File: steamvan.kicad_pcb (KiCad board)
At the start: 2 copper layers, 243.4 x 76.7 mm, 168 parts, among them J1 Conn_01x05_Male, Q1 FMMT493TA, SW1 SW_Push, U1 STM32F303CBTx, U2 TLV70233_SOT23-5, U3 NUF2221W1T2G, Y1 8MHz

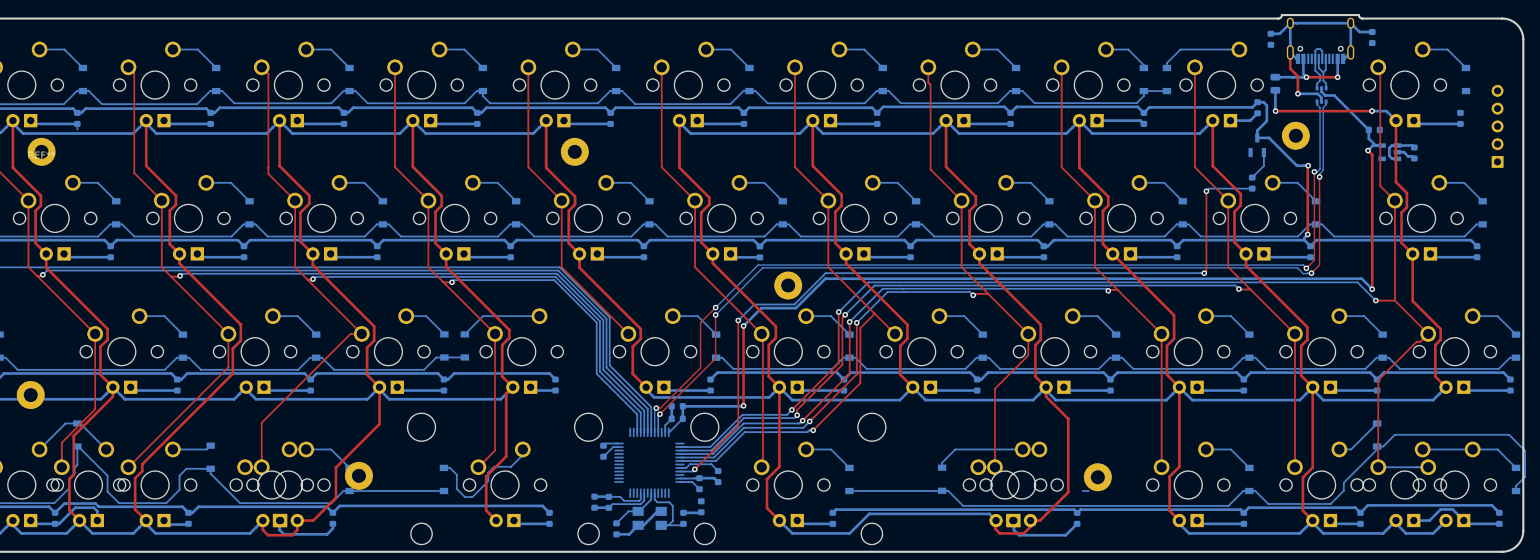
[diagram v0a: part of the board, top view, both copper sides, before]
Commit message: Update: Add schematic components for RGB underglow, and work on routing
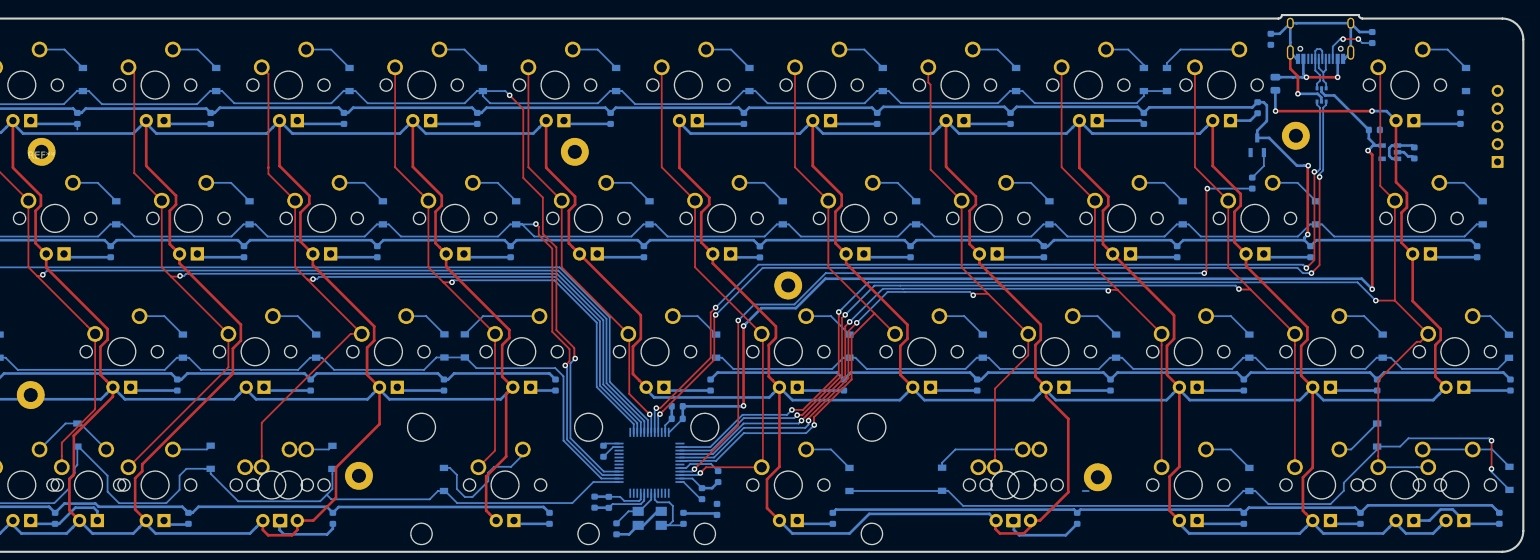
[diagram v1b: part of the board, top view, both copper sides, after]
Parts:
- moved D40 3.99 mm to (144.4, 118.3)
- moved C9 2.29 mm to (199.4, 125.7)
- moved C3 1.47 mm to (197.2, 123.5)
- moved D36 1.01 mm to (312.5, 102.4)
- moved D46 0.95 mm to (312.6, 121.3)
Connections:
- U1 pad 13: COL1 -> ROW3
- U1 pad 14: Net-(U1-Pad14) -> ROW2
- U1 pad 15: Net-(U1-Pad15) -> ROW1
- U1 pad 16: COL5 -> ROW0
- U1 pad 17: COL7 -> RGBLED_3V3
- U1 pad 18: ROW0 -> Net-(U1-Pad18)
- U1 pad 19: ROW1 -> Net-(U1-Pad19)
- U1 pad 20: ROW2 -> Net-(U1-Pad20)
- U1 pad 26: Net-(U1-Pad26) -> COL4
- U1 pad 27: COL4 -> COL3
- U1 pad 28: COL3 -> COL2
- U1 pad 29: COL2 -> COL1
- U1 pad 30: COL1 -> COL0
- U1 pad 31: COL0 -> COL5
- U1 pad 46: Net-(U1-Pad46) -> COL6
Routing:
- net ROW0: track 188.1 -> 254.2 mm, vias 0 -> 2
- net ROW1: track 232.5 -> 278.0 mm, vias 0 -> 2
- net ROW2: track 193.1 -> 226.7 mm
- net ROW3: track 198.4 -> 225.7 mm, vias 0 -> 2
- net COL5: track 44.0 -> 59.4 mm, vias 0 -> 1
- net COL6: track 63.2 -> 75.4 mm, vias 0 -> 1
- net Net-(RC7-Pad2): track 0.00 -> 8.06 mm, vias 0 -> 2
- net Net-(D40-Pad2): track 9.66 -> 6.34 mm
- net GND: track 71.8 -> 74.8 mm
- net Net-(D36-Pad2): track 7.28 -> 6.28 mm
- net Net-(D46-Pad2): track 14.4 -> 13.4 mm
- net +3V3: track 173.1 -> 174.1 mm
- net COL11: track 187.8 -> 188.7 mm

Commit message: Update: Work on underglow
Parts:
- added C12: 100n, Capacitor_SMD:C_0603_1608Metric, B.Cu at (153.0, 111.5)
- added C13: 100n, Capacitor_SMD:C_0603_1608Metric, B.Cu at (100.2, 113.4)
- added C14: 100n, Capacitor_SMD:C_0603_1608Metric, B.Cu at (98.3, 78.2)
- added C15: 100n, Capacitor_SMD:C_0603_1608Metric, B.Cu at (138.3, 78.0)
- added C16: 100n, Capacitor_SMD:C_0603_1608Metric, B.Cu at (195.6, 77.9)
- added C17: 100n, Capacitor_SMD:C_0603_1608Metric, B.Cu at (234.6, 77.5)
- added C18: 100n, Capacitor_SMD:C_0603_1608Metric, B.Cu at (271.8, 78.2)
- added C19: 100n, Capacitor_SMD:C_0603_1608Metric, B.Cu at (284.6, 113.8)
- added C20: 100n, Capacitor_SMD:C_0603_1608Metric, B.Cu at (231.4, 116.0)
- added RC9: 470, Resistor_SMD:R_0603_1608Metric, B.Cu at (166.8, 114.2)
- added RGB1: WS2812B, LED_SMD:LED_WS2812B_PLCC4_5.0x5.0mm_P3.2mm, B.Cu at (150.0, 115.6)
- added RGB2: WS2812B, LED_SMD:LED_WS2812B_PLCC4_5.0x5.0mm_P3.2mm, B.Cu at (94.7, 114.8)
- added RGB3: WS2812B, LED_SMD:LED_WS2812B_PLCC4_5.0x5.0mm_P3.2mm, B.Cu at (92.8, 79.0)
- added RGB4: WS2812B, LED_SMD:LED_WS2812B_PLCC4_5.0x5.0mm_P3.2mm, B.Cu at (132.7, 78.9)
- added RGB5: WS2812B, LED_SMD:LED_WS2812B_PLCC4_5.0x5.0mm_P3.2mm, B.Cu at (190.0, 79.0)
- added RGB6: WS2812B, LED_SMD:LED_WS2812B_PLCC4_5.0x5.0mm_P3.2mm, B.Cu at (228.5, 79.0)
- added RGB7: WS2812B, LED_SMD:LED_WS2812B_PLCC4_5.0x5.0mm_P3.2mm, B.Cu at (266.3, 79.0)
- added RGB8: WS2812B, LED_SMD:LED_WS2812B_PLCC4_5.0x5.0mm_P3.2mm, B.Cu at (278.1, 114.3)
- added RGB9: WS2812B, LED_SMD:LED_WS2812B_PLCC4_5.0x5.0mm_P3.2mm, B.Cu at (225.9, 119.5)
- added U4: 74LVC1G34, Package_TO_SOT_SMD:SOT-353_SC-70-5, B.Cu at (175.8, 118.6)
- moved Q1 13.4 mm to (289.6, 77.0), turned to 270 degrees
- moved D20 1.13 mm to (227.6, 84.5)
- moved D15 1.11 mm to (132.6, 84.5)
- moved D22 1.11 mm to (265.9, 84.5)
- moved D18 0.98 mm to (189.7, 84.3)
- moved D13 0.98 mm to (92.1, 84.3)
- moved Y1 0.38 mm to (189.7, 127.4)
- moved C1 0.36 mm to (185.0, 128.1)
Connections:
- U1 pad 4: ROW3 -> Net-(U1-Pad4)
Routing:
- net Net-(RGB1-Pad2): track 0.00 -> 64.2 mm
- net GND: track 74.8 -> 135.1 mm
- net Net-(RGB4-Pad2): track 0.00 -> 53.6 mm
- net Net-(RGB2-Pad2): track 0.00 -> 44.6 mm, vias 0 -> 2
- net Net-(RGB3-Pad2): track 0.00 -> 36.4 mm
- net Net-(RGB5-Pad2): track 0.00 -> 34.9 mm
- net Net-(RGB6-Pad2): track 0.00 -> 34.3 mm
- net RGBLED: track 0.00 -> 20.7 mm
- net Net-(Q1-Pad1): track 4.26 -> 15.8 mm
- net Net-(RC9-Pad2): track 0.00 -> 10.7 mm
- net +5V: track 1298.2 -> 1307.4 mm
- net RGBLED_3V3: track 0.00 -> 9.07 mm, vias 0 -> 2
- net Net-(RC6-Pad2): track 0.00 -> 8.20 mm, vias 0 -> 2
- net ROW1: track 278.0 -> 270.3 mm
- net LEDGND: track 833.7 -> 836.7 mm, vias 2 -> 3
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
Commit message: Update: Work on routing
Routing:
- net Net-(RGB7-Pad2): track 0.00 -> 59.6 mm, vias 0 -> 2
- net Net-(RGB8-Pad2): track 0.00 -> 59.4 mm
- net ROW2: track 226.7 -> 250.6 mm, vias 0 -> 2
- net GND: track 135.1 -> 157.3 mm
- net +5V: track 1307.4 -> 1324.9 mm
- net LEDPWM: track 111.9 -> 112.5 mm

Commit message: Update: More work on routing
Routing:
- net SWCLK: track 0.00 -> 160.4 mm, vias 0 -> 2
- net Net-(RC8-Pad1): track 12.4 -> 154.0 mm, vias 0 -> 2
- net +5V: track 1324.9 -> 1309.8 mm
- net COL1: track 168.1 -> 177.7 mm

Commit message: Update: More routing
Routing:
- net NRST: track 0.00 -> 179.1 mm, vias 0 -> 1
- net +3V3: track 174.2 -> 346.2 mm, vias 4 -> 10
- net SWDIO: track 0.00 -> 159.3 mm, vias 0 -> 3
- net LEDGND: track 836.7 -> 976.5 mm, vias 3 -> 12
- net GND: track 157.3 -> 277.0 mm, vias 1 -> 5
- net ROW0: track 254.2 -> 299.0 mm, vias 2 -> 4
- net ROW3: track 225.9 -> 261.5 mm, vias 2 -> 4
- net +5V: track 1309.8 -> 1326.4 mm, vias 2 -> 4
- net Net-(D41-Pad2): track 18.2 -> 12.4 mm
- net Net-(RGB3-Pad2): track 36.4 -> 37.9 mm
- net Net-(RGB7-Pad2): track 59.6 -> 58.8 mm
- net Net-(K_Q1-Pad4): track 7.66 -> 6.86 mm
- net COL11: track 189.0 -> 188.3 mm
- net COL10: track 159.7 -> 160.3 mm

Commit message: Update: Finish routing
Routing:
- net GND: track 277.0 -> 629.9 mm, vias 5 -> 28
- net +5V: track 1326.4 -> 1330.8 mm, vias 4 -> 5
- net NRST: track 179.1 -> 180.0 mm
- net D_N: track 133.9 -> 133.3 mm

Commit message: Update: Work on ground plane
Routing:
- net +5V: track 1330.8 -> 1340.2 mm
- net COL10: track 160.3 -> 164.2 mm
- net COL9: track 140.1 -> 141.8 mm
- net COL7: track 85.0 -> 86.6 mm
- net COL11: track 188.5 -> 189.9 mm
- net COL2: track 152.2 -> 153.4 mm
- net COL1: track 177.7 -> 178.7 mm
- net COL8: track 126.3 -> 127.2 mm
- net GND: vias 28 -> 87
- added copper zone on B.Cu, net GND
- added copper zone on F.Cu, net GND

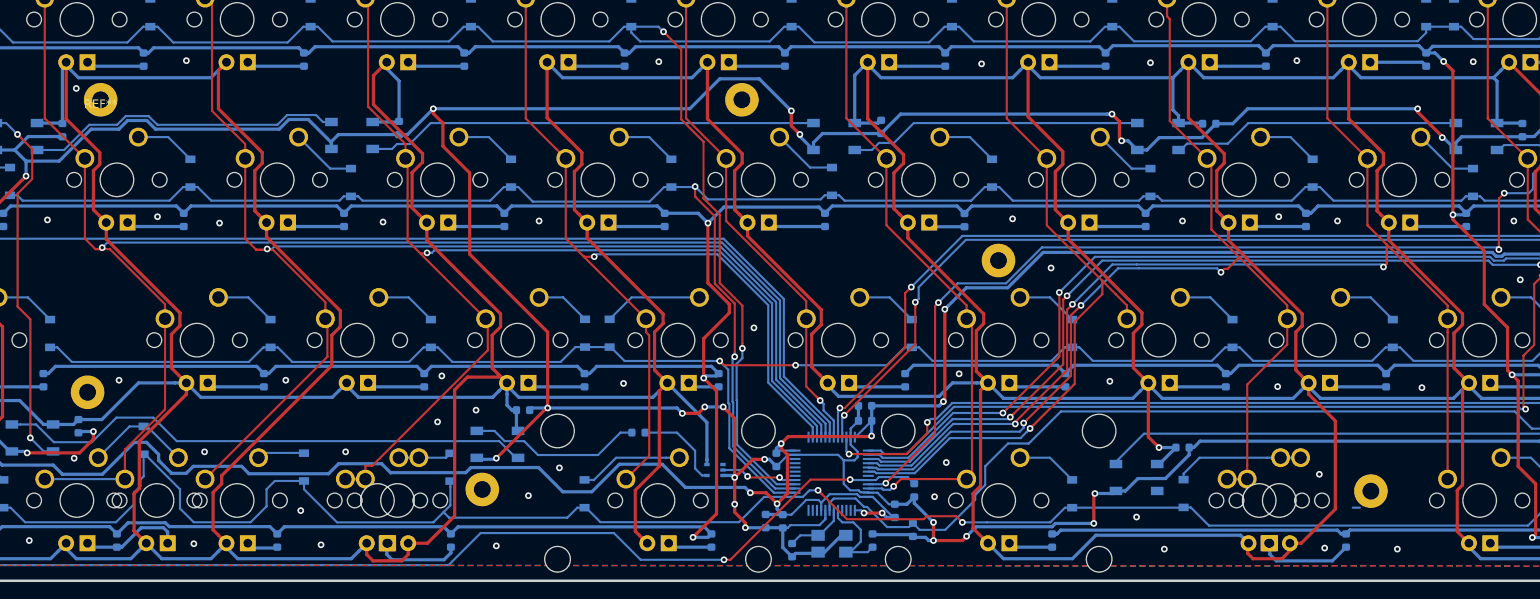
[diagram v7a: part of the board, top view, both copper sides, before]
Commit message: Update: Work on ground plane and exclusion around MCU
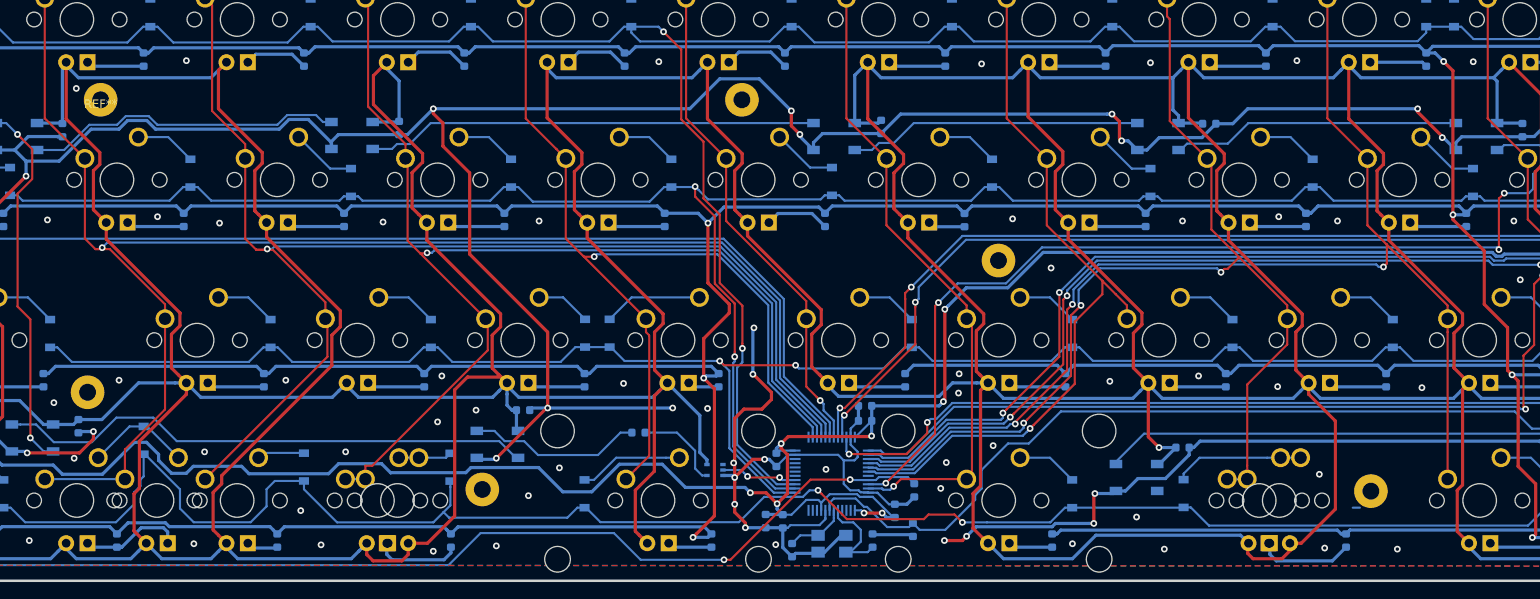
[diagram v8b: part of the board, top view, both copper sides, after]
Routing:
- net GND: track 629.9 -> 626.1 mm, vias 87 -> 95
- net COL8: track 127.2 -> 128.7 mm
- net Net-(K_T1-Pad4): track 6.86 -> 7.86 mm
- net Net-(K_R1-Pad4): track 6.86 -> 7.86 mm
- net Net-(K_E1-Pad4): track 6.86 -> 7.86 mm
- net COL9: track 141.8 -> 142.7 mm
- net Net-(K_G1-Pad4): track 6.86 -> 7.76 mm
- net Net-(K_W1-Pad4): track 6.86 -> 7.65 mm
